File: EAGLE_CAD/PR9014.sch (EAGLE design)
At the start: 70 parts, among them J1 M3_SCREW_POST

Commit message: Updated Library
Added AO3435, (Fet for reverse polarity) to the library and replaced it
in the sch and layout.
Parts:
- removed FET1: SI2333DDS, PubRadioLib:SI2333DDS
- added FET2: AO3435, PR_Parts_Library:AO3435
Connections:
- net GND: now also FET2.GATE; no longer FET1.GATE
- net N$34: now also FET2.DRAIN; no longer FET1.DRAIN
- net VCC: now also FET2.SOURCE; no longer FET1.SOURCE
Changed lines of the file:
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@@
 <part name="GND2" library="SparkFun-Aesthetics" deviceset="GND" device=""/>
 <part name="GND12" library="SparkFun-Aesthetics" deviceset="GND" device=""/>
-<part name="FET1" library="PubRadioLib" deviceset="SI2333DDS" device=""/>
 <part name="GND3" library="SparkFun-Aesthetics" deviceset="GND" device=""/>
 <part name="MCU" library="SparkFun-DigitalIC" deviceset="ATTINY45" device="TINY85-20-SMT" value="Tiny45-20-SMT"/>
@@
 <part name="C17" library="resistor" deviceset="C-US" device="C0402" value="1uf"/>
 <part name="C9" library="resistor" deviceset="C-US" device="C0402" value="1uF"/>
+<part name="FET2" library="PR_Parts_Library" deviceset="AO3435" device=""/>
 </parts>
 <sheets>
@@
 <instance part="GND2" gate="1" x="-35.56" y="111.76"/>
 <instance part="GND12" gate="1" x="55.88" y="127"/>
-<instance part="FET1" gate="G$1" x="-20.32" y="129.54" rot="R270"/>
 <instance part="GND3" gate="1" x="-27.94" y="129.54"/>
 <instance part="MCU" gate="G$1" x="175.26" y="124.46"/>
@@
 </instance>
 <instance part="C9" gate="G$1" x="88.9" y="30.48" rot="R90"/>
+<instance part="FET2" gate="G$1" x="-20.32" y="129.54" rot="R270"/>
 </instances>
 <busses>
@@
 </segment>
 <segment>
-<pinref part="FET1" gate="G$1" pin="GATE"/>
 <pinref part="GND3" gate="1" pin="GND"/>
 <wire x1="-25.4" y1="132.08" x2="-27.94" y2="132.08" width="0.1524" layer="91"/>
+<pinref part="FET2" gate="G$1" pin="GATE"/>
 </segment>
 <segment>
@@
 </segment>
 <segment>
-<pinref part="FET1" gate="G$1" pin="SOURCE"/>
 <pinref part="P+1" gate="VCC" pin="VCC"/>
 <wire x1="-25.4" y1="127" x2="-35.56" y2="127" width="0.1524" layer="91"/>
@@
 <pinref part="C1" gate="G$1" pin="P$1"/>
 <junction x="-35.56" y="127"/>
+<pinref part="FET2" gate="G$1" pin="SOURCE"/>
 </segment>
 <segment>
@@
 <segment>
 <pinref part="R1" gate="G$1" pin="SW_IN"/>
-<pinref part="FET1" gate="G$1" pin="DRAIN"/>
 <wire x1="-12.7" y1="127" x2="-12.7" y2="129.54" width="0.1524" layer="91"/>
-</segment>
-</net>
+<pinref part="FET2" gate="G$1" pin="DRAIN"/>
+</segment>
+</net>

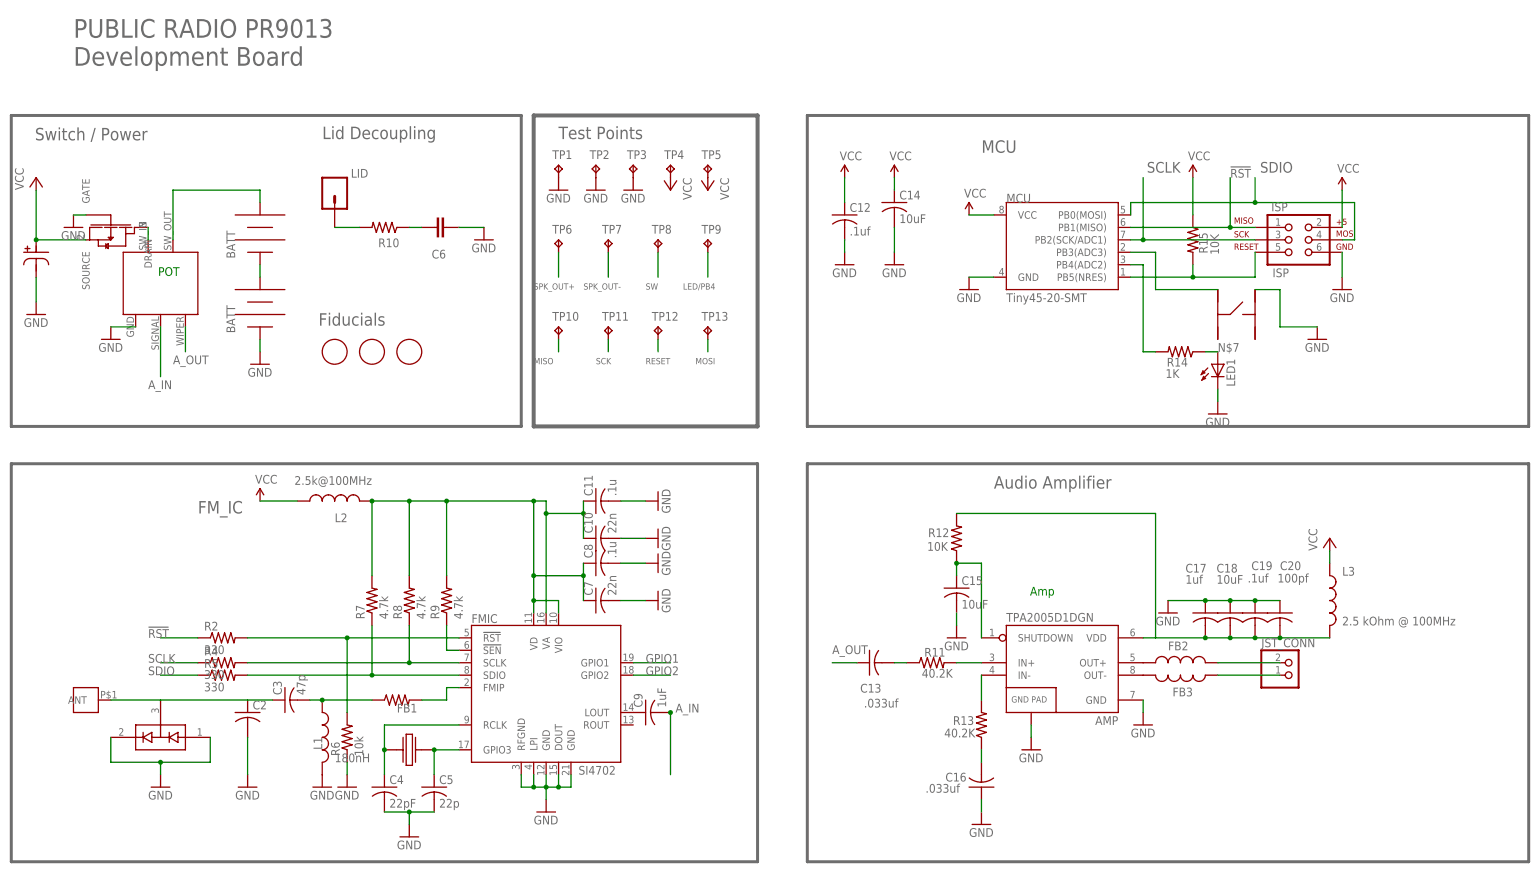
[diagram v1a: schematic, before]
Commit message: bunch of changes
couple library updates, the most notable of which is the button
footprint

then

a bunch of layout edits
mostly in response to andy’s feedback
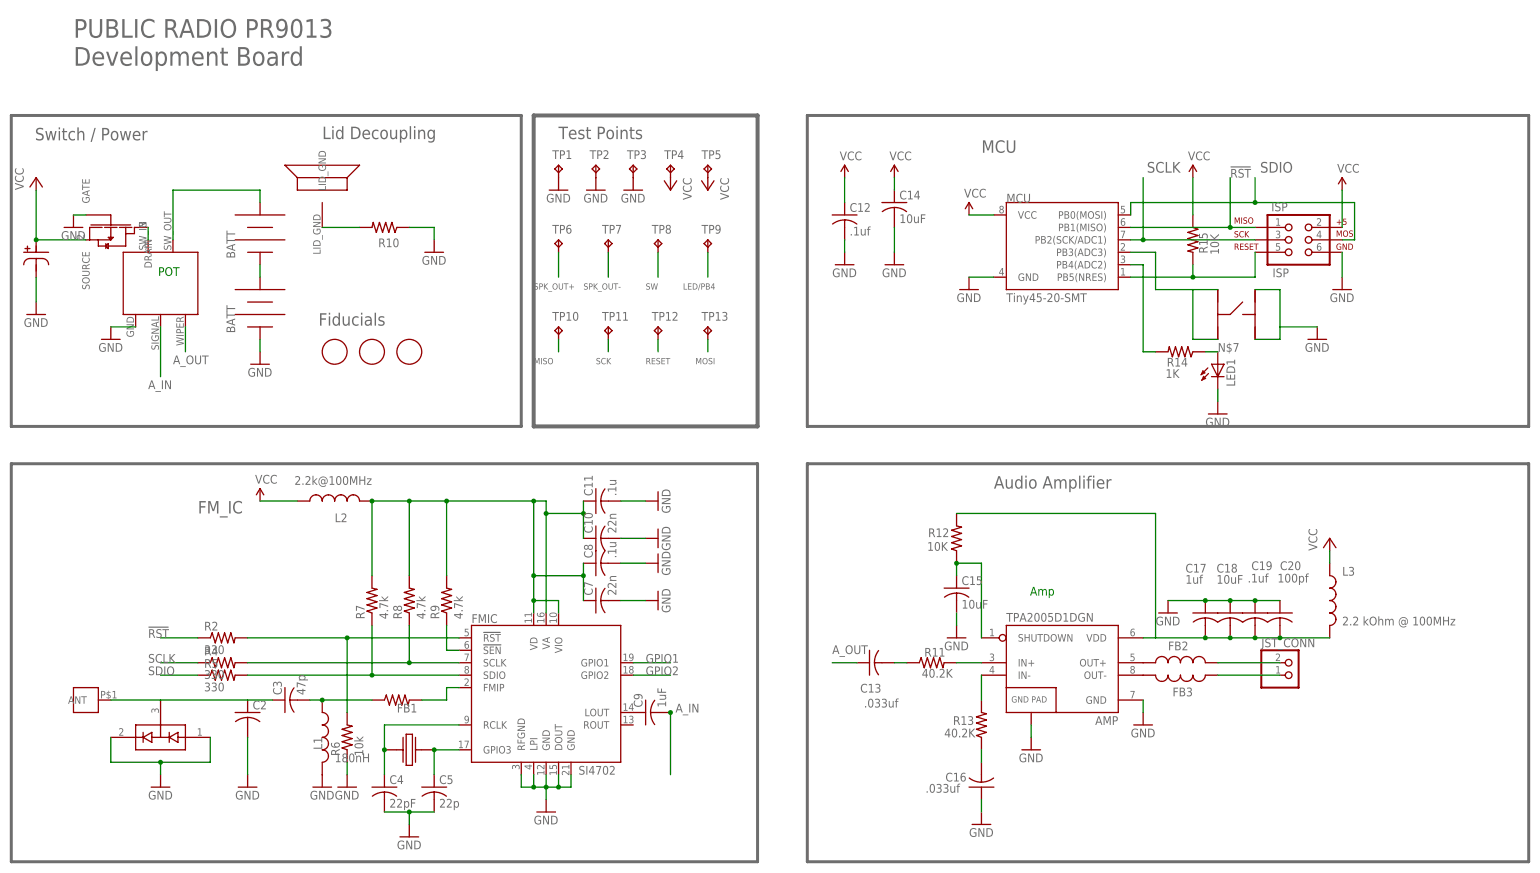
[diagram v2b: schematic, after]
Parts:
- removed C6: (no value), SparkFun-Passives:CAP0805
- removed LID: M01PTH, SparkFun-Connectors:M01PTH
- added SW1: C&K_PTS645, PR_Parts_Library:C&K_PTS645
- L2: value 2.5k@100MHz -> 2.2k@100MHz; device SparkFun-Passives:INDUCTOR0603 -> SparkFun-Passives:INDUCTOR0402
- L3: value 2.5 kOhm @ 100MHz -> 2.2 kOhm @ 100MHz; device SparkFun-Passives:INDUCTOR0603 -> SparkFun-Passives:INDUCTOR0402
- R10: device resistor:R-US_R0402 -> resistor:R-US_R0805
- U$1: value C&KPTS6465 -> (none); device PR_Parts_Library:C&KPTS6465 -> PR_Parts_Library:CE32A_FOR_JST
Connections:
- removed net N$35: C6.1, R10.1
- net GND: now also R10.1, SW1.P$1, SW1.P$2; no longer C6.2, U$1.P$1
- net N$8: now also U$1.LID_GND; no longer LID.1
- net SW: now also SW1.P$3, SW1.P$4; no longer U$1.P$3
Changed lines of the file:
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@@
 <part name="GND28" library="SparkFun-Aesthetics" deviceset="GND" device=""/>
 <part name="GND7" library="SparkFun-Aesthetics" deviceset="GND" device=""/>
-<part name="L2" library="SparkFun-Passives" deviceset="INDUCTOR" device="0603" value="2.5k@100MHz"/>
-<part name="L3" library="SparkFun-Passives" deviceset="INDUCTOR" device="0603" value="2.5 kOhm @ 100MHz"/>
+<part name="L2" library="SparkFun-Passives" deviceset="INDUCTOR" device="0402" value="2.2k@100MHz"/>
+<part name="L3" library="SparkFun-Passives" deviceset="INDUCTOR" device="0402" value="2.2 kOhm @ 100MHz"/>
 <part name="P+2" library="supply1" deviceset="VCC" device=""/>
 <part name="GND29" library="SparkFun-Aesthetics" deviceset="GND" device=""/>
@@
 <part name="C19" library="resistor" deviceset="C-US" device="C0402" value=".1uf"/>
 <part name="C20" library="resistor" deviceset="C-US" device="C0402" value="100pf"/>
-<part name="LID" library="SparkFun-Connectors" deviceset="M01" device="PTH"/>
-<part name="C6" library="SparkFun-Passives" deviceset="CAP" device="0805"/>
-<part name="R10" library="resistor" deviceset="R-US_" device="R0402"/>
+<part name="R10" library="resistor" deviceset="R-US_" device="R0805"/>
 <part name="D1" library="SparkFun-DiscreteSemi" deviceset="BAV99" device=""/>
 <part name="JP5" library="PR_Parts_Library" deviceset="BK-92_MPD_AA_BATT_CLIP" device=""/>
@@
 <part name="C10" library="resistor" deviceset="C-US" device="C0402" value="22n"/>
 <part name="C11" library="resistor" deviceset="C-US" device="C0402" value=".1u"/>
-<part name="U$1" library="PR_Parts_Library" deviceset="C&amp;KPTS6465" device=""/>
+<part name="SW1" library="PR_Parts_Library" deviceset="C&amp;K_PTS645" device=""/>
 <part name="C1" library="PR_Parts_Library" deviceset="NICHICON_SERIESUD" device="" value="220uF"/>
 <part name="TP1" library="testpad" deviceset="TP" device="TP14R"/>
@@
 <part name="C9" library="resistor" deviceset="C-US" device="C0402" value="1uF"/>
 <part name="FET2" library="PR_Parts_Library" deviceset="AO3435" device=""/>
+<part name="U$1" library="PR_Parts_Library" deviceset="CE32A_FOR_JST" device=""/>
 </parts>
 <sheets>
@@
 <instance part="GND5" gate="1" x="-20.32" y="106.68"/>
 <instance part="GND2" gate="1" x="-35.56" y="111.76"/>
-<instance part="GND12" gate="1" x="55.88" y="127"/>
+<instance part="GND12" gate="1" x="45.72" y="124.46"/>
 <instance part="GND3" gate="1" x="-27.94" y="129.54"/>
 <instance part="MCU" gate="G$1" x="175.26" y="124.46"/>
@@
 <attribute name="VALUE" x="217.932" y="57.023" size="1.778" layer="96"/>
 </instance>
-<instance part="LID" gate="G$1" x="25.4" y="137.16" smashed="yes" rot="R270">
-<attribute name="NAME" x="28.702" y="139.7" size="1.778" layer="95"/>
-</instance>
-<instance part="C6" gate="G$1" x="48.26" y="129.54" smashed="yes" rot="R90">
-<attribute name="NAME" x="48.133" y="124.968" size="1.778" layer="95" rot="R180"/>
-<attribute name="VALUE" x="48.133" y="132.334" size="1.778" layer="96" rot="R90"/>
-</instance>
 <instance part="R10" gate="G$1" x="35.56" y="129.54" smashed="yes" rot="R180">
 <attribute name="NAME" x="34.29" y="125.5014" size="1.778" layer="95"/>
@@
 <instance part="C10" gate="G$1" x="78.74" y="66.04" rot="R90"/>
 <instance part="C11" gate="G$1" x="78.74" y="73.66" rot="R90"/>
-<instance part="U$1" gate="G$1" x="210.82" y="111.76" rot="R270"/>
+<instance part="SW1" gate="G$1" x="210.82" y="111.76" rot="R270"/>
 <instance part="C1" gate="G$1" x="-35.56" y="124.46"/>
 <instance part="TP1" gate="G$1" x="71.12" y="142.24"/>
@@
 <instance part="C9" gate="G$1" x="88.9" y="30.48" rot="R90"/>
 <instance part="FET2" gate="G$1" x="-20.32" y="129.54" rot="R270"/>
+<instance part="U$1" gate="G$1" x="22.86" y="132.08" rot="R90"/>
 </instances>
 <busses>
@@
 </segment>
 <segment>
-<pinref part="GND12" gate="1" pin="GND"/>
-<wire x1="55.88" y1="129.54" x2="50.8" y2="129.54" width="0.1524" layer="91"/>
-<pinref part="C6" gate="G$1" pin="2"/>
-</segment>
-<segment>
 <pinref part="GND3" gate="1" pin="GND"/>
 <wire x1="-25.4" y1="132.08" x2="-27.94" y2="132.08" width="0.1524" layer="91"/>
@@
 <wire x1="226.06" y1="109.22" x2="218.44" y2="109.22" width="0.1524" layer="91"/>
 <wire x1="218.44" y1="109.22" x2="218.44" y2="116.84" width="0.1524" layer="91"/>
-<pinref part="U$1" gate="G$1" pin="P$1"/>
+<pinref part="SW1" gate="G$1" pin="P$1"/>
 <wire x1="218.44" y1="116.84" x2="213.36" y2="116.84" width="0.1524" layer="91"/>
+<pinref part="SW1" gate="G$1" pin="P$2"/>
+<wire x1="213.36" y1="106.68" x2="218.44" y2="106.68" width="0.1524" layer="91"/>
+<wire x1="218.44" y1="106.68" x2="218.44" y2="109.22" width="0.1524" layer="91"/>
 </segment>
 <segment>
@@
 <pinref part="TP3" gate="G$1" pin="TP"/>
 <pinref part="GND14" gate="1" pin="GND"/>
+</segment>
+<segment>
+<pinref part="R10" gate="G$1" pin="1"/>
+<pinref part="GND12" gate="1" pin="GND"/>
+<wire x1="40.64" y1="129.54" x2="45.72" y2="129.54" width="0.1524" layer="91"/>
+<wire x1="45.72" y1="129.54" x2="45.72" y2="127" width="0.1524" layer="91"/>
 </segment>
 </net>
@@
 </segment>
 </net>
-<net name="N$35" class="0">
-<segment>
-<pinref part="R10" gate="G$1" pin="1"/>
-<pinref part="C6" gate="G$1" pin="1"/>
-<wire x1="40.64" y1="129.54" x2="43.18" y2="129.54" width="0.1524" layer="91"/>
-</segment>
-</net>
 <net name="A_IN" class="0">
 <segment>
@@
 </segment>
 </net>
-<net name="N$8" class="0">
-<segment>
-<pinref part="LID" gate="G$1" pin="1"/>
-<wire x1="25.4" y1="129.54" x2="30.48" y2="129.54" width="0.1524" layer="91"/>
-<pinref part="R10" gate="G$1" pin="2"/>
-</segment>
-</net>
 <net name="SW" class="0">
 <segment>
-<wire x1="205.74" y1="116.84" x2="193.04" y2="116.84" width="0.1524" layer="91"/>
+<wire x1="205.74" y1="116.84" x2="200.66" y2="116.84" width="0.1524" layer="91"/>
+<wire x1="200.66" y1="116.84" x2="193.04" y2="116.84" width="0.1524" layer="91"/>
 <wire x1="193.04" y1="116.84" x2="193.04" y2="124.46" width="0.1524" layer="91"/>
 <pinref part="MCU" gate="G$1" pin="PB3(ADC3)"/>
 <wire x1="193.04" y1="124.46" x2="187.96" y2="124.46" width="0.1524" layer="91"/>
-<pinref part="U$1" gate="G$1" pin="P$3"/>
+<pinref part="SW1" gate="G$1" pin="P$3"/>
+<pinref part="SW1" gate="G$1" pin="P$4"/>
+<wire x1="205.74" y1="106.68" x2="200.66" y2="106.68" width="0.1524" layer="91"/>
+<wire x1="200.66" y1="106.68" x2="200.66" y2="116.84" width="0.1524" layer="91"/>
 </segment>
 <segment>
@@
 </segment>
 </net>
+<net name="N$8" class="0">
+<segment>
+<pinref part="U$1" gate="G$1" pin="LID_GND"/>
+<pinref part="R10" gate="G$1" pin="2"/>
+<wire x1="22.86" y1="129.54" x2="30.48" y2="129.54" width="0.1524" layer="91"/>
+</segment>
+</net>

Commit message: bunch of routing stuff
and made the test points larger

pretty close to being released for this round
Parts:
- added TP14, TP15, TP16, TP17, TP18: TPTP20R, testpad:TPTP20R
- FB2, FB3, L1: device SparkFun-Passives:INDUCTOR0603 -> SparkFun-Passives:INDUCTOR0805
- TP1, TP10, TP11, TP12, TP13, TP2, TP3, TP4, TP5, TP6, TP7, TP8, TP9: value TPTP14R -> TPTP20R; device testpad:TPTP14R -> testpad:TPTP20R
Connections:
- removed net N$14: C2.1, C3.1, D1.COM, J1.ANT
- removed net N$15: JP5.POS, R1.SW_OUT
- removed net N$2: C5.1, FMIC.GPIO3, U$6.P$1
- removed net N$34: FET2.DRAIN, R1.SW_IN
- new net ANT: C2.1, C3.1, D1.COM, J1.ANT, TP18.TP
- new net N$10: C5.1, FMIC.GPIO3, U$6.P$4
- new net SW_IN: FET2.DRAIN, R1.SW_IN, TP14.TP
- new net SW_OUT: JP5.POS, R1.SW_OUT, TP15.TP
- net A_IN: now also TP16.TP
- net A_OUT: now also TP17.TP
- net N$1: now also U$6.P$1; no longer U$6.P$4
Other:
- moved on the sheet: TP1, TP10, TP11, TP12, TP13, TP2, TP3, TP4, TP5, TP6, TP7, TP8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

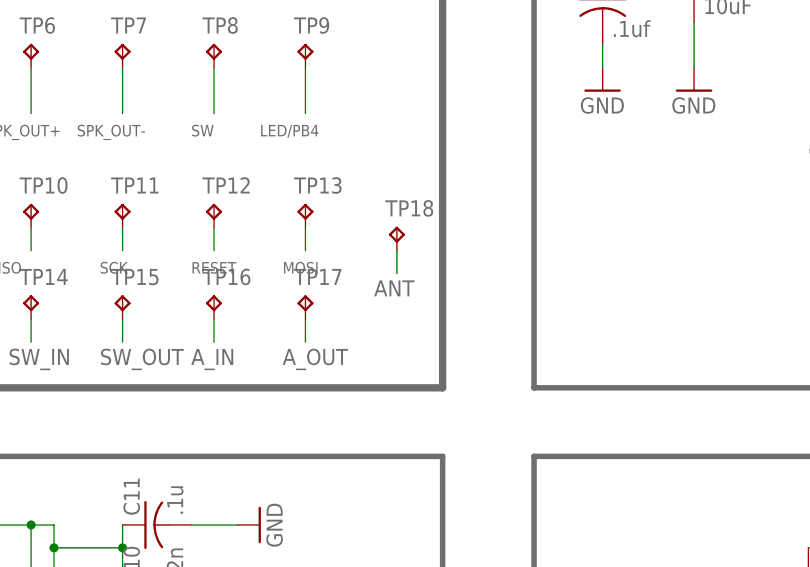
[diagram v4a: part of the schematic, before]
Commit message: Updated Layout and Library
Updated C1s package (it was a little fat)
Added vias around the edge of the board, Spk, and front end
Smoothed out a couple traces (audio, antenna test pad)
Changed battery silk to bottom layer.
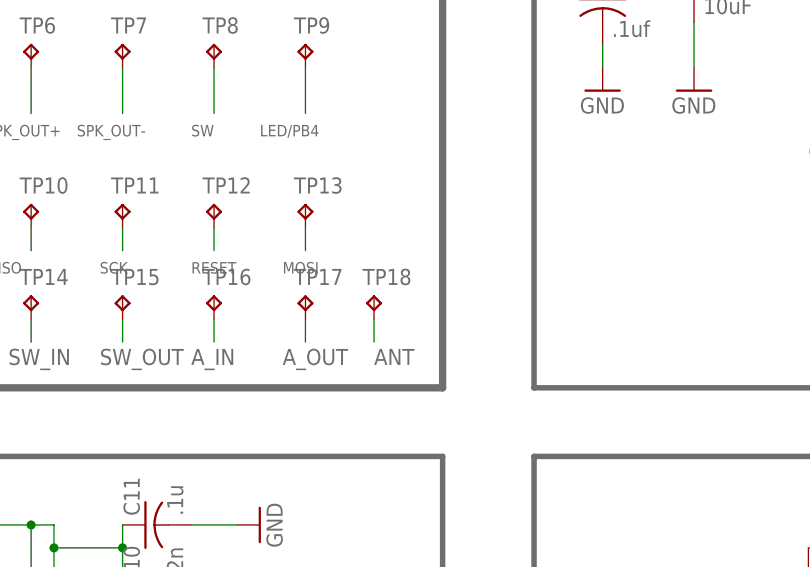
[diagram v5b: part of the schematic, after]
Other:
- moved on the sheet: TP18
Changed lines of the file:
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@@
 <instance part="TP16" gate="G$1" x="86.36" y="99.06"/>
 <instance part="TP17" gate="G$1" x="96.52" y="99.06"/>
-<instance part="TP18" gate="G$1" x="106.68" y="106.68"/>
+<instance part="TP18" gate="G$1" x="104.14" y="99.06"/>
 </instances>
 <busses>
@@
 <segment>
 <pinref part="TP18" gate="G$1" pin="TP"/>
-<wire x1="106.68" y1="104.14" x2="106.68" y2="101.6" width="0.1524" layer="91"/>
-<label x="104.14" y="99.06" size="1.778" layer="95"/>
-</segment>
-</net>
+<wire x1="104.14" y1="96.52" x2="104.14" y2="93.98" width="0.1524" layer="91"/>
+<label x="104.14" y="91.44" size="1.778" layer="95"/>
+</segment>
+</net>

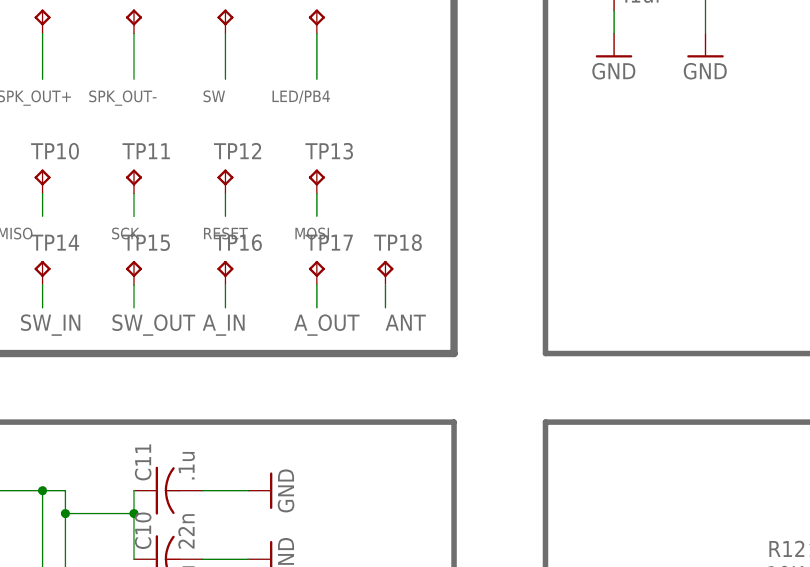
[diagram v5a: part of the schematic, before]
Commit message: Updated Layout
Fixed a few things, including some notes from Andy.
Todo: change gnu pad connection on speaker screw
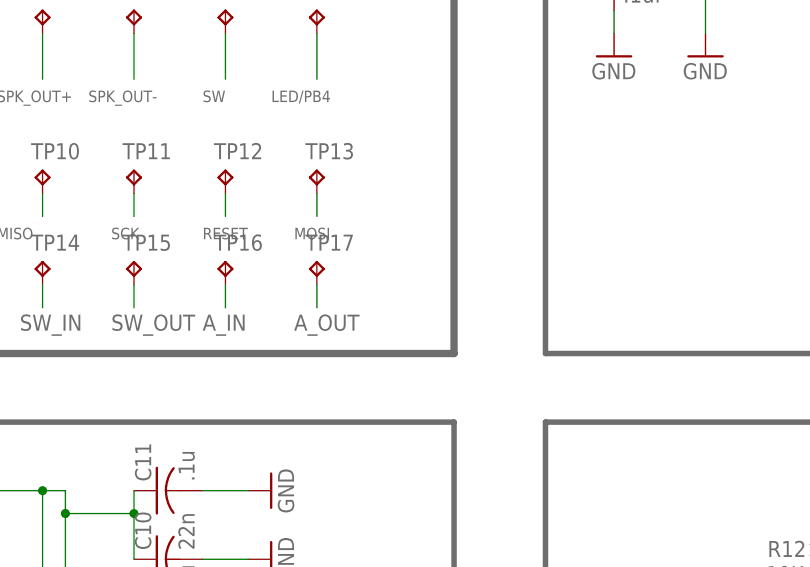
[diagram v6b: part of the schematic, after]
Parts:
- removed TP18: TPTP20R, testpad:TPTP20R
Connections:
- net ANT: no longer TP18.TP
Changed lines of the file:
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@@
 <part name="TP16" library="testpad" deviceset="TP" device="TP20R" value="TPTP20R"/>
 <part name="TP17" library="testpad" deviceset="TP" device="TP20R" value="TPTP20R"/>
-<part name="TP18" library="testpad" deviceset="TP" device="TP20R" value="TPTP20R"/>
 </parts>
 <sheets>
@@
 <instance part="TP16" gate="G$1" x="86.36" y="99.06"/>
 <instance part="TP17" gate="G$1" x="96.52" y="99.06"/>
-<instance part="TP18" gate="G$1" x="104.14" y="99.06"/>
 </instances>
 <busses>
@@
 <label x="-20.32" y="40.64" size="1.778" layer="95" rot="R180"/>
 </segment>
-<segment>
-<pinref part="TP18" gate="G$1" pin="TP"/>
-<wire x1="104.14" y1="96.52" x2="104.14" y2="93.98" width="0.1524" layer="91"/>
-<label x="104.14" y="91.44" size="1.778" layer="95"/>
-</segment>
-</net>
+</net>
